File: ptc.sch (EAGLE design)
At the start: 2 parts

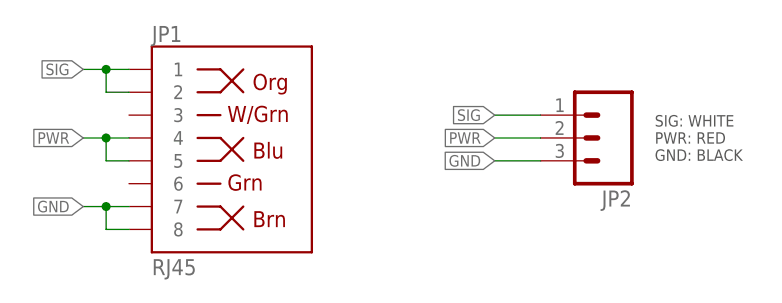
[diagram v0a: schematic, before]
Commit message: Replaced thru holes with custom Eagle component that had larger thru holes. Adjusted cut out section. Added PCB images rendered by OSHPark. Added README.md.
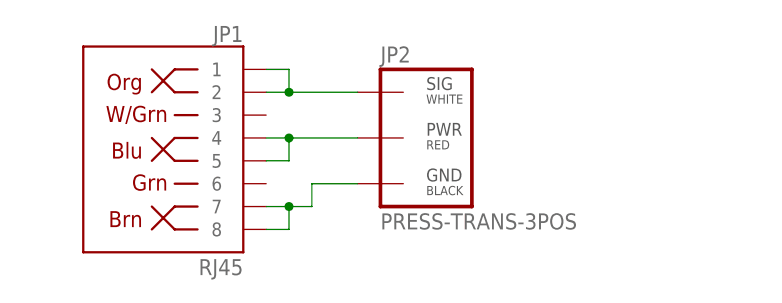
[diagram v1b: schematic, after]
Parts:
- JP2: value (none) -> PRESS-TRANS-3POS; device SparkFun-Connectors:M03PTH -> SDSURocket-Connectors:PRESS-TRANS-3POS
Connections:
- net GND renamed N$3
- net PWR renamed N$2
- net SIG renamed N$1
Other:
- note removed: "SIG: WHITE PWR: RED GND: BLACK"
- moved on the sheet: JP1, JP2
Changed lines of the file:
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@@
 <setting verticaltext="up"/>
 </settings>
-<grid distance="0.1" unitdist="inch" unit="inch" style="dots" multiple="1" display="yes" altdistance="0.01" altunitdist="inch" altunit="inch"/>
+<grid distance="0.1" unitdist="inch" unit="inch" style="lines" multiple="1" display="no" altdistance="0.01" altunitdist="inch" altunit="inch"/>
 <layers>
 <layer number="1" name="Top" color="4" fill="1" visible="no" active="no"/>
@@
 <layer number="223" name="223bmp" color="24" fill="1" visible="no" active="no"/>
 <layer number="224" name="224bmp" color="25" fill="1" visible="no" active="no"/>
+<layer number="225" name="225bmp" color="7" fill="1" visible="yes" active="yes"/>
+<layer number="226" name="226bmp" color="7" fill="1" visible="yes" active="yes"/>
+<layer number="227" name="227bmp" color="7" fill="1" visible="yes" active="yes"/>
+<layer number="228" name="228bmp" color="7" fill="1" visible="yes" active="yes"/>
+<layer number="229" name="229bmp" color="7" fill="1" visible="yes" active="yes"/>
+<layer number="230" name="230bmp" color="7" fill="1" visible="yes" active="yes"/>
+<layer number="231" name="231bmp" color="7" fill="1" visible="yes" active="yes"/>
 <layer number="248" name="Housing" color="7" fill="1" visible="yes" active="yes"/>
 <layer number="249" name="Edge" color="7" fill="1" visible="yes" active="yes"/>
@@
 <parts>
 <part name="JP1" library="SparkFun-Connectors" deviceset="RJ45-8" device="PTH" value="RJ45"/>
-<part name="JP2" library="SparkFun-Connectors" deviceset="M03" device="PTH"/>
+<part name="JP2" library="SDSURocket-Connectors" deviceset="PRESS-TRANS-3POS" device=""/>
 </parts>
 <sheets>
 <sheet>
 <plain>
-<text x="76.2" y="20.32" size="1.27" layer="97" align="center-left">SIG: WHITE
-PWR: RED
-GND: BLACK</text>
 </plain>
 <instances>
-<instance part="JP1" gate="JP1" x="25.4" y="20.32"/>
-<instance part="JP2" gate="G$1" x="71.12" y="20.32" rot="R180"/>
+<instance part="JP1" gate="JP1" x="25.4" y="20.32" rot="MR0"/>
+<instance part="JP2" gate="G$1" x="48.26" y="20.32"/>
 </instances>
 <busses>
 </busses>
 <nets>
-<net name="SIG" class="0">
+<net name="N$1" class="0">
 <segment>
+<pinref part="JP1" gate="JP1" pin="2"/>
+<pinref part="JP2" gate="G$1" pin="1"/>
+<wire x1="33.02" y1="25.4" x2="35.56" y2="25.4" width="0.1524" layer="91"/>
 <pinref part="JP1" gate="JP1" pin="1"/>
-<wire x1="17.78" y1="27.94" x2="15.24" y2="27.94" width="0.1524" layer="91"/>
-<pinref part="JP1" gate="JP1" pin="2"/>
-<wire x1="15.24" y1="27.94" x2="12.7" y2="27.94" width="0.1524" layer="91"/>
-<wire x1="17.78" y1="25.4" x2="15.24" y2="25.4" width="0.1524" layer="91"/>
-<wire x1="15.24" y1="25.4" x2="15.24" y2="27.94" width="0.1524" layer="91"/>
-<junction x="15.24" y="27.94"/>
-<label x="12.7" y="27.94" size="1.27" layer="95" rot="MR0" xref="yes"/>
-</segment>
-<segment>
-<pinref part="JP2" gate="G$1" pin="1"/>
-<wire x1="63.5" y1="22.86" x2="58.42" y2="22.86" width="0.1524" layer="91"/>
-<label x="58.42" y="22.86" size="1.27" layer="95" rot="MR0" xref="yes"/>
+<wire x1="35.56" y1="25.4" x2="43.18" y2="25.4" width="0.1524" layer="91"/>
+<wire x1="33.02" y1="27.94" x2="35.56" y2="27.94" width="0.1524" layer="91"/>
+<wire x1="35.56" y1="27.94" x2="35.56" y2="25.4" width="0.1524" layer="91"/>
+<junction x="35.56" y="25.4"/>
 </segment>
 </net>
-<net name="PWR" class="0">
+<net name="N$2" class="0">
 <segment>
 <pinref part="JP1" gate="JP1" pin="4"/>
-<wire x1="17.78" y1="20.32" x2="15.24" y2="20.32" width="0.1524" layer="91"/>
+<pinref part="JP2" gate="G$1" pin="2"/>
+<wire x1="33.02" y1="20.32" x2="35.56" y2="20.32" width="0.1524" layer="91"/>
 <pinref part="JP1" gate="JP1" pin="5"/>
-<wire x1="15.24" y1="20.32" x2="12.7" y2="20.32" width="0.1524" layer="91"/>
-<wire x1="17.78" y1="17.78" x2="15.24" y2="17.78" width="0.1524" layer="91"/>
-<wire x1="15.24" y1="17.78" x2="15.24" y2="20.32" width="0.1524" layer="91"/>
-<junction x="15.24" y="20.32"/>
-<label x="12.7" y="20.32" size="1.27" layer="95" rot="MR0" xref="yes"/>
-</segment>
-<segment>
-<pinref part="JP2" gate="G$1" pin="2"/>
-<wire x1="63.5" y1="20.32" x2="58.42" y2="20.32" width="0.1524" layer="91"/>
-<label x="58.42" y="20.32" size="1.27" layer="95" rot="MR0" xref="yes"/>
+<wire x1="35.56" y1="20.32" x2="43.18" y2="20.32" width="0.1524" layer="91"/>
+<wire x1="33.02" y1="17.78" x2="35.56" y2="17.78" width="0.1524" layer="91"/>
+<wire x1="35.56" y1="17.78" x2="35.56" y2="20.32" width="0.1524" layer="91"/>
+<junction x="35.56" y="20.32"/>
 </segment>
 </net>
-<net name="GND" class="0">
+<net name="N$3" class="0">
 <segment>
 <pinref part="JP1" gate="JP1" pin="7"/>
-<wire x1="17.78" y1="12.7" x2="15.24" y2="12.7" width="0.1524" layer="91"/>
+<wire x1="33.02" y1="12.7" x2="35.56" y2="12.7" width="0.1524" layer="91"/>
+<wire x1="35.56" y1="12.7" x2="38.1" y2="12.7" width="0.1524" layer="91"/>
+<wire x1="38.1" y1="12.7" x2="38.1" y2="15.24" width="0.1524" layer="91"/>
+<pinref part="JP2" gate="G$1" pin="3"/>
+<wire x1="38.1" y1="15.24" x2="43.18" y2="15.24" width="0.1524" layer="91"/>
 <pinref part="JP1" gate="JP1" pin="8"/>
-<wire x1="15.24" y1="12.7" x2="12.7" y2="12.7" width="0.1524" layer="91"/>
-<wire x1="17.78" y1="10.16" x2="15.24" y2="10.16" width="0.1524" layer="91"/>
-<wire x1="15.24" y1="10.16" x2="15.24" y2="12.7" width="0.1524" layer="91"/>
-<junction x="15.24" y="12.7"/>
-<label x="12.7" y="12.7" size="1.27" layer="95" rot="MR0" xref="yes"/>
-</segment>
-<segment>
-<pinref part="JP2" gate="G$1" pin="3"/>
-<wire x1="63.5" y1="17.78" x2="58.42" y2="17.78" width="0.1524" layer="91"/>
-<label x="58.42" y="17.78" size="1.27" layer="95" rot="MR0" xref="yes"/>
+<wire x1="33.02" y1="10.16" x2="35.56" y2="10.16" width="0.1524" layer="91"/>
+<wire x1="35.56" y1="10.16" x2="35.56" y2="12.7" width="0.1524" layer="91"/>
+<junction x="35.56" y="12.7"/>
 </segment>
 </net>
@@
 </schematic>
 </drawing>
-<compatibility>
-<note version="6.3" minversion="6.2.2" severity="warning">
-Since Version 6.2.2 text objects can contain more than one line,
-which will not be processed correctly with this version.
-</note>
-</compatibility>
 </eagle>
